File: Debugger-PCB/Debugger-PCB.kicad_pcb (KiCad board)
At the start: 2 copper layers, 64.8 x 48.1 mm, 56 parts, among them J1 Conn_01x04, J2 Conn_01x04, J3 Conn_01x02, J4 USB_C_Receptacle_USB2.0, SW3 SW_Push, SW4 SW_Push, SW5 SW_Push, U1 HX9193, U2 HX9193, U3 CH340E, U4 TJA1051T-3, U5 STM32F103RCTx, U6 XPT2046TS, U7 W25Q32JVSS, Y1 12M

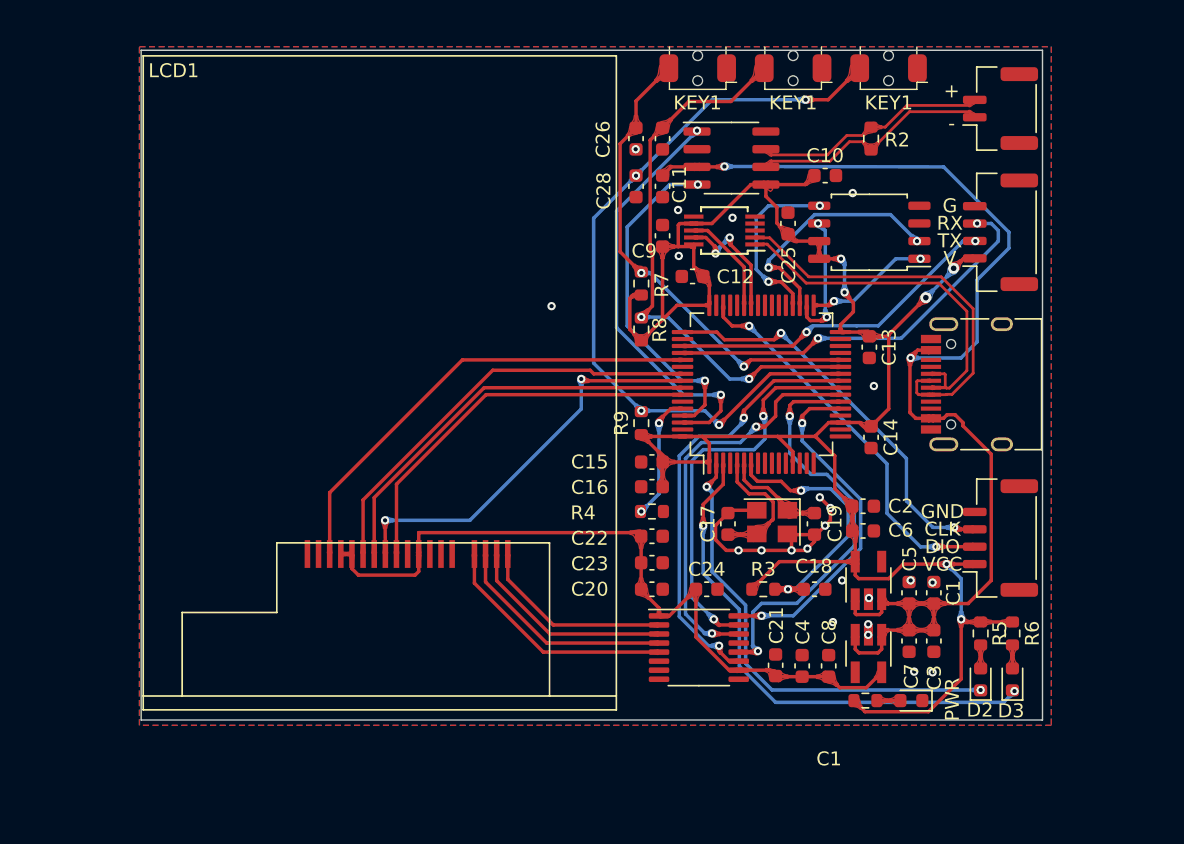
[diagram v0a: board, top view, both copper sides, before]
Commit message: fix some details of PCB
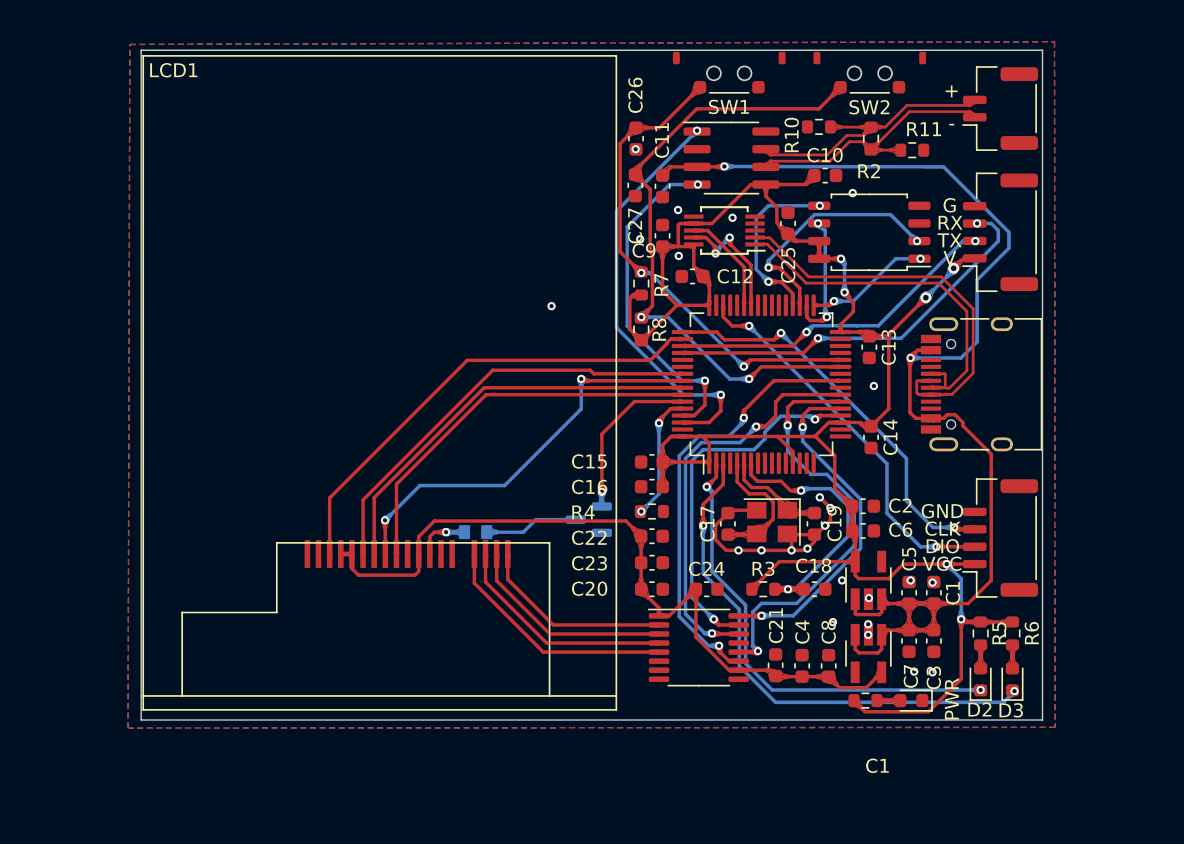
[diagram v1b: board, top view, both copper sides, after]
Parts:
- removed  : 100n, Capacitor_SMD:C_0603_1608Metric
- removed C28: 100n, Capacitor_SMD:C_0603_1608Metric
- removed R9: 1k, Resistor_SMD:R_0603_1608Metric
- removed SW5: SW_Push, MyLib:SW_YD-3410
- added C27: 100n, Capacitor_SMD:C_0603_1608Metric, F.Cu at (152.5, 93.3)
- added Q1: S8050, Package_TO_SOT_SMD:SOT-23, B.Cu at (149.1, 117.3)
- added R10: 10k, Resistor_SMD:R_0603_1608Metric, F.Cu at (165.7, 89.1)
- added R11: 10k, Resistor_SMD:R_0603_1608Metric, F.Cu at (172.4, 90.8)
- added R12: R, GENERAL_RCL_SMD:L0603(1608M), B.Cu at (141.0, 118.2)
- SW1: renamed from SW3; footprint MyLib:SW_YD-3410 -> debugger:button
- SW2: renamed from SW4; footprint MyLib:SW_YD-3410 -> debugger:button
- moved SW2 5.52 mm to (169.3, 85.2)
- moved SW1 2.30 mm to (159.2, 85.2)
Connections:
- LCD1 pad 3: GND -> /TFT/LED-
- U5 pad 20: unconnected-(U5-Pad20) -> /MCU/TOUCH_CS
- U5 pad 24: /MCU/TOUCH_CS -> unconnected-(U5-Pad24)
- U5 pad 26: /Key&LED/KEY3 -> /MCU/KEY3
- U5 pad 50: unconnected-(U5-Pad50) -> /MCU/LCD_CS
- U5 pad 53: /MCU/LCD_CS -> unconnected-(U5-Pad53)
- U5 pad 59: unconnected-(U5-Pad59) -> /MCU/LCD_LED
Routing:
- net /Key&LED/KEY3: track 55.1 -> 0.00 mm, vias 4 -> 0
- net /MCU/LCD_LED: track 0.00 -> 12.0 mm, vias 0 -> 1
- net Net-(Q1-Pad3): track 0.00 -> 6.76 mm
- net /Key&LED/KEY2: track 40.0 -> 45.1 mm
- net /TFT/LED-: track 0.00 -> 3.87 mm, vias 0 -> 1
- net VCC: track 150.1 -> 146.8 mm
- net /Power&Port/CAN+: track 16.8 -> 19.7 mm
- net /MCU/TOUCH_CS: track 28.6 -> 26.5 mm
- net /Power&Port/CAN-: track 17.3 -> 19.5 mm
- net LCD_3V3: track 54.3 -> 55.2 mm
- net /Key&LED/KEY1: track 34.2 -> 34.8 mm
- net GND: vias 23 -> 24
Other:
- board text removed: "KEY1"

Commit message: Finish the GUI
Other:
- board text added: "V2.0"
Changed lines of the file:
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@@
     )
     (fp_line (start -1.4 -1.4) (end 1.4 -1.4) (layer "F.SilkS") (width 0.12))
-    (fp_circle (center -1.1 0) (end -0.6 0) (layer "Edge.Cuts") (width 0.12) (fill none))
-    (fp_circle (center 1.1 0) (end 1.6 0) (layer "Edge.Cuts") (width 0.12) (fill none))
-    (fp_line (start 4.1 -1.7) (end 4.1 2.1) (layer "F.CrtYd") (width 0.05))
-    (fp_line (start -4.1 2.1) (end 4.1 2.1) (layer "F.CrtYd") (width 0.05))
+    (fp_circle (center 1.1 0.1) (end 1.6 0.1) (layer "Edge.Cuts") (width 0.12) (fill none))
+    (fp_circle (center -1.1 0.1) (end -0.6 0.1) (layer "Edge.Cuts") (width 0.12) (fill none))
     (fp_line (start -4.1 -1.7) (end -4.1 2.1) (layer "F.CrtYd") (width 0.05))
     (fp_line (start -4.1 -1.7) (end 4.1 -1.7) (layer "F.CrtYd") (width 0.05))
+    (fp_line (start -4.1 2.1) (end 4.1 2.1) (layer "F.CrtYd") (width 0.05))
+    (fp_line (start 4.1 -1.7) (end 4.1 2.1) (layer "F.CrtYd") (width 0.05))
     (fp_line (start -1.5 2.032) (end -1.5 1.3) (layer "User.1") (width 0.12))
     (fp_line (start -1.5 2.032) (end 1.5 2.032) (layer "User.1") (width 0.12))
+    (fp_line (start -3.5 1.1) (end 3.5 1.1) (layer "User.1") (width 0.12))
     (fp_line (start 1.5 2.032) (end 1.5 1.3) (layer "User.1") (width 0.12))
-    (fp_line (start -3.5 1.1) (end 3.5 1.1) (layer "User.1") (width 0.12))
     (pad "1" smd roundrect (at -2.1 -1 180) (size 0.9 0.9) (layers "F.Cu" "F.Paste" "F.Mask") (roundrect_rratio 0.25)
       (net 2 "GND") (pinfunction "1") (pintype "passive"))
@@
     )
     (fp_line (start -1.4 -1.4) (end 1.4 -1.4) (layer "F.SilkS") (width 0.12))
-    (fp_circle (center -1.1 0) (end -0.6 0) (layer "Edge.Cuts") (width 0.12) (fill none))
-    (fp_circle (center 1.1 0) (end 1.6 0) (layer "Edge.Cuts") (width 0.12) (fill none))
+    (fp_circle (center -1.1 0.1) (end -0.6 0.1) (layer "Edge.Cuts") (width 0.12) (fill none))
+    (fp_circle (center 1.1 0.1) (end 1.6 0.1) (layer "Edge.Cuts") (width 0.12) (fill none))
+    (fp_line (start -4.1 -1.7) (end -4.1 2.1) (layer "F.CrtYd") (width 0.05))
+    (fp_line (start 4.1 -1.7) (end 4.1 2.1) (layer "F.CrtYd") (width 0.05))
+    (fp_line (start -4.1 -1.7) (end 4.1 -1.7) (layer "F.CrtYd") (width 0.05))
     (fp_line (start -4.1 2.1) (end 4.1 2.1) (layer "F.CrtYd") (width 0.05))
-    (fp_line (start -4.1 -1.7) (end -4.1 2.1) (layer "F.CrtYd") (width 0.05))
-    (fp_line (start -4.1 -1.7) (end 4.1 -1.7) (layer "F.CrtYd") (width 0.05))
-    (fp_line (start 4.1 -1.7) (end 4.1 2.1) (layer "F.CrtYd") (width 0.05))
+    (fp_line (start -1.5 2.032) (end -1.5 1.3) (layer "User.1") (width 0.12))
+    (fp_line (start -1.5 2.032) (end 1.5 2.032) (layer "User.1") (width 0.12))
     (fp_line (start 1.5 2.032) (end 1.5 1.3) (layer "User.1") (width 0.12))
-    (fp_line (start -1.5 2.032) (end 1.5 2.032) (layer "User.1") (width 0.12))
     (fp_line (start -3.5 1.1) (end 3.5 1.1) (layer "User.1") (width 0.12))
-    (fp_line (start -1.5 2.032) (end -1.5 1.3) (layer "User.1") (width 0.12))
     (pad "1" smd roundrect (at -2.1 -1 180) (size 0.9 0.9) (layers "F.Cu" "F.Paste" "F.Mask") (roundrect_rratio 0.25)
       (net 2 "GND") (pinfunction "1") (pintype "passive"))
@@
     (effects (font (size 1 1) (thickness 0.15)))
   )
+  (gr_text "V2.0" (at 154.025 130.8) (layer "F.SilkS")
+    (effects (font (size 1 1) (thickness 0.15)))
+  )

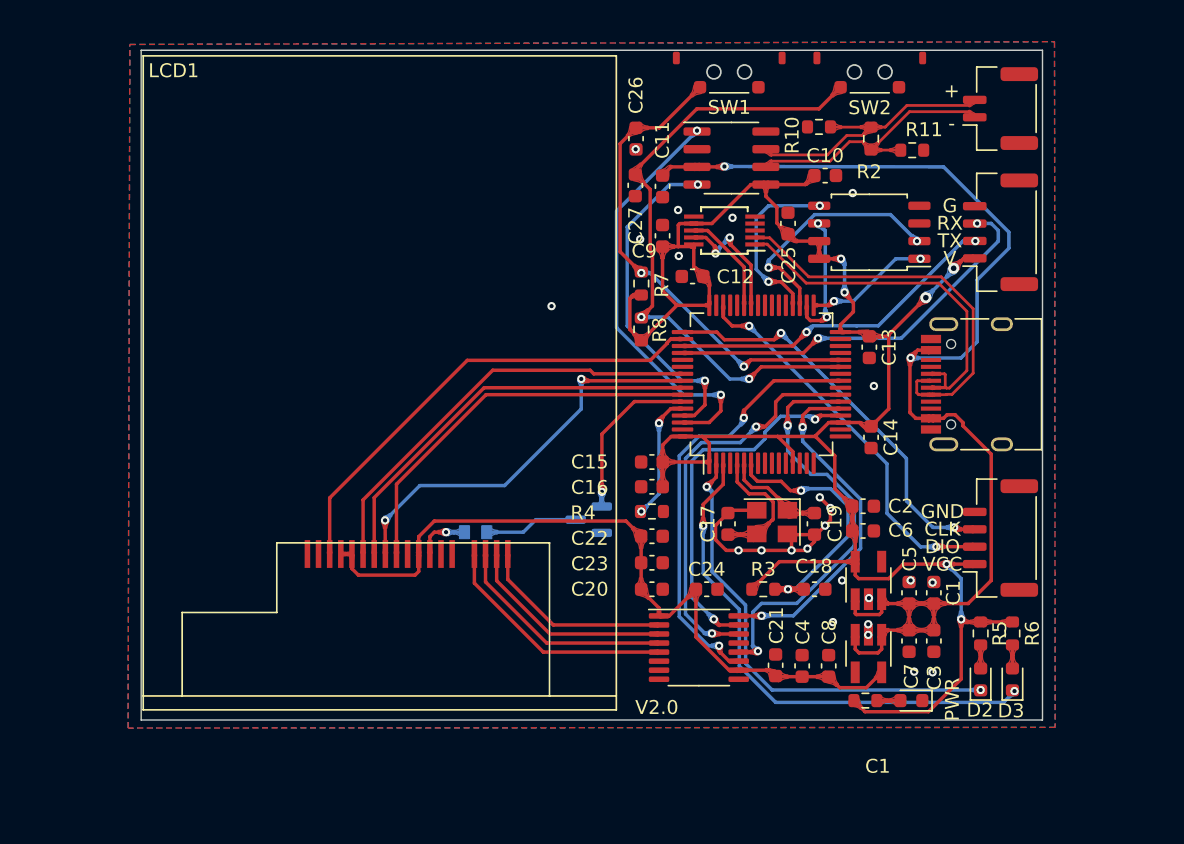
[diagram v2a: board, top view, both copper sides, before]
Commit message: change the file name debugger-code into debugger_code_f103. Change the stm32f103rct6 into stm32f407vet6. Add file debugger_code_f407
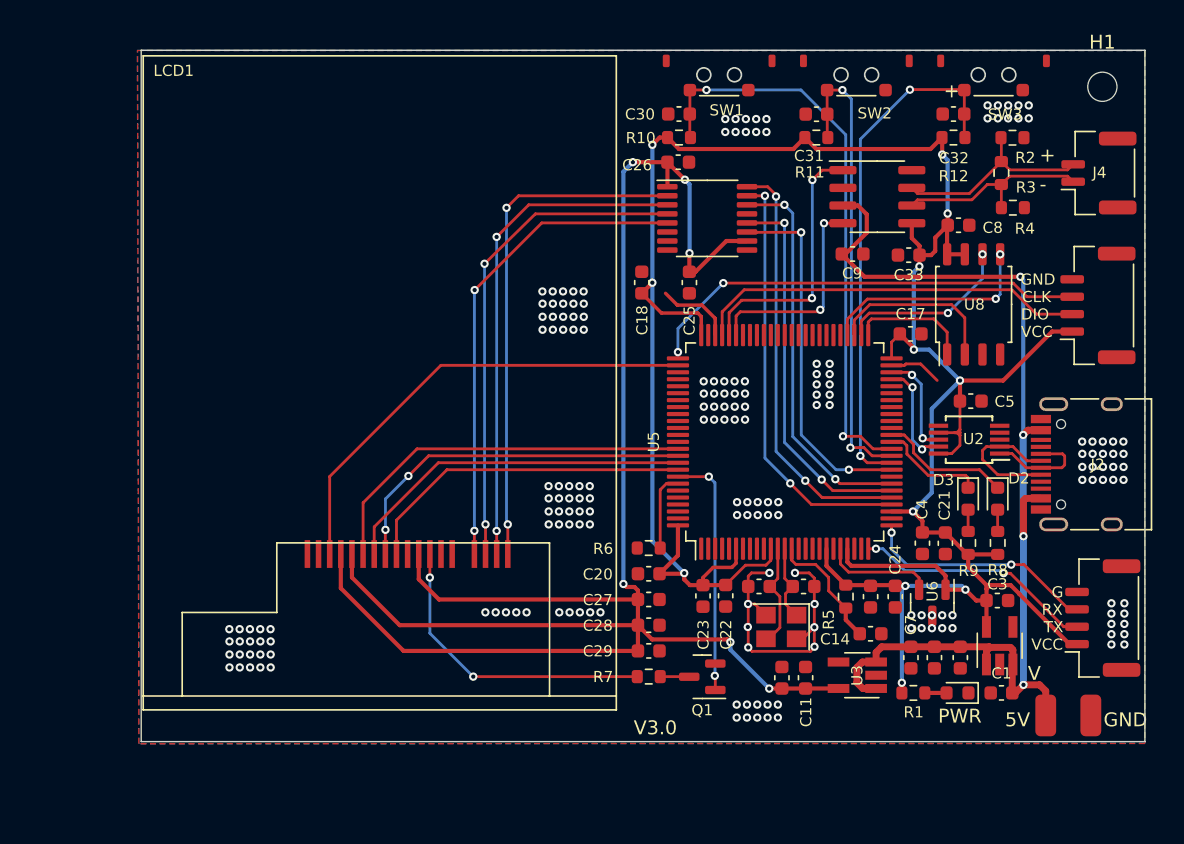
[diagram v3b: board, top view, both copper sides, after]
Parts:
- removed C15, C16: 100n, Capacitor_SMD:C_0603_1608Metric
- added ?: , , F.Cu at (182.0, 131.4)
- added ?: , , F.Cu at (185.2, 131.4)
- added C28: 100n, Capacitor_SMD:C_0603_1608Metric, F.Cu at (153.4, 124.9)
- added C29: 100n, Capacitor_SMD:C_0603_1608Metric, F.Cu at (153.4, 126.7)
- added C30: 100n, Capacitor_SMD:C_0603_1608Metric, F.Cu at (155.6, 88.2)
- added C31: 100n, Capacitor_SMD:C_0603_1608Metric, F.Cu at (165.5, 88.2)
- added C32: 100n, Capacitor_SMD:C_0603_1608Metric, F.Cu at (175.3, 88.2)
- added C33: 100n, Capacitor_SMD:C_0603_1608Metric, F.Cu at (172.1, 98.3)
- added H1: mountinghole, MountingHole:MountingHole_2.1mm, F.Cu at (186.0, 86.2)
- added R9: 1k, Resistor_SMD:R_0603_1608Metric, F.Cu at (176.4, 119.0)
- added SW3: SW_Push, debugger:button, F.Cu at (178.2, 85.4)
- added U8: W25Q32JVSS, Package_SO:SOIC-8_5.23x5.23mm_P1.27mm, F.Cu at (176.8, 101.8)
- C11, C6: value 100n -> 10u
- C12, C13: value 100n -> 12p
- C17, C19: value 12p -> 100n
- C2, C3: value 10u -> 100n
- J2: value Conn_01x04 -> USB_C_Receptacle_USB2.0; footprint Connector_JST:JST_GH_SM04B-GHS-TB_1x04-1MP_P1.25mm_Horizontal -> Connector_USB:USB_C_Receptacle_HRO_TYPE-C-31-M-12
- J3: value Conn_01x02 -> Conn_01x04; footprint Connector_JST:JST_GH_SM02B-GHS-TB_1x02-1MP_P1.25mm_Horizontal -> Connector_JST:JST_GH_SM04B-GHS-TB_1x04-1MP_P1.25mm_Horizontal
- J4: value USB_C_Receptacle_USB2.0 -> Conn_01x02; footprint Connector_USB:USB_C_Receptacle_HRO_TYPE-C-31-M-12 -> Connector_JST:JST_GH_SM02B-GHS-TB_1x02-1MP_P1.25mm_Horizontal
- Q1: moved to F.Cu
- R10, R11: value 10k -> 1k
- R12: value R -> 1k; footprint GENERAL_RCL_SMD:L0603(1608M) -> Resistor_SMD:R_0603_1608Metric; moved to F.Cu
- R2: value 120 -> 10k
- R3: value 10k -> 120
- R5: value 1k -> 10k
- R6: value 1k -> 10K
- R7: value 1k -> R
- U2: value HX9193 -> CH340E; footprint Package_TO_SOT_SMD:SOT-23-5_HandSoldering -> Package_SO:MSOP-10_3x3mm_P0.5mm
- U3: value CH340E -> HX9193; footprint Package_SO:MSOP-10_3x3mm_P0.5mm -> Package_TO_SOT_SMD:SOT-23-5_HandSoldering
- U5: value STM32F103RCTx -> STM32F407VETx; footprint Package_QFP:LQFP-64_10x10mm_P0.5mm -> Package_QFP:LQFP-100_14x14mm_P0.5mm
- U6: value XPT2046TS -> REF3030; footprint debugger:TSSOP-16_4.4x5mm_P0.65mm -> Package_TO_SOT_SMD:SOT-23
- U7: value W25Q32JVSS -> XPT2046TS; footprint Package_SO:SOIC-8_5.23x5.23mm_P1.27mm -> debugger:TSSOP-16_4.4x5mm_P0.65mm
- moved R12 44.5 mm to (175.3, 89.8)
- moved C11 36.8 mm to (164.7, 128.7), turned to 90 degrees
- moved C10 36.2 mm to (163.0, 128.7), turned to 90 degrees
- moved R3 34.5 mm to (178.8, 92.4), turned to -90 degrees
- moved R4 33.9 mm to (179.6, 94.9)
- moved U3 33.4 mm to (168.4, 128.5)
- moved C8 33.0 mm to (175.7, 96.1), turned to 0 degrees
- moved R8 29.9 mm to (178.5, 119.0)
- moved C27 29.8 mm to (153.4, 123.0), turned to 0 degrees
- moved J1 28.7 mm to (186.1, 124.4)
- moved R7 28.3 mm to (153.4, 128.6), turned to 0 degrees
- moved R6 26.8 mm to (153.4, 119.3), turned to 0 degrees
- moved C18 25.3 mm to (152.9, 100.3), turned to 90 degrees
- moved C12 23.7 mm to (164.6, 122.1), turned to 0 degrees
- moved C17 18.9 mm to (172.3, 104.0), turned to 0 degrees
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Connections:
- C10 pad 1: VCC -> LCD_3V3
- C11 pad 1: +5V -> LCD_3V3
- C12 pad 1: VCC -> /MCU/OSC_OUT
- C13 pad 1: VCC -> /MCU/OSC_IN
- C14 pad 1: VCC -> GND
- C14 pad 2: GND -> Net-(U5-NRST)
- C17 pad 1: /MCU/OSC_IN -> VCC
- C18 pad 1: GND -> VCC
- C18 pad 2: Net-(C18-Pad2) -> GND
- C19 pad 1: /MCU/OSC_OUT -> VCC
- C2 pad 1: VCC -> +5V
- C20 pad 1: LCD_3V3 -> VCC
- C21 pad 1: LCD_3V3 -> VCC
- C22 pad 1: LCD_3V3 -> VCC
- C23 pad 1: LCD_3V3 -> VCC
- C24 pad 1: LCD_3V3 -> VCC
- C25 pad 1: VCC -> LCD_3V3
- C26 pad 1: /Key&LED/KEY1 -> LCD_3V3
- C27 pad 1: /Key&LED/KEY2 -> LCD_3V3
- C3 pad 1: +5V -> VCC
- C4 pad 1: LCD_3V3 -> VCC
- C5 pad 1: +5V -> VCC
- C6 pad 1: VCC -> +5V
- C8 pad 1: LCD_3V3 -> VCC
- C9 pad 1: VCC -> +5V
- D2 pad 2: Net-(D2-Pad2) -> Net-(D2-A)
- D3 pad 2: Net-(D3-Pad2) -> Net-(D3-A)
- J3 pad 1: /Power&Port/CAN- -> VCC
- J3 pad 2: /Power&Port/CAN+ -> /MCU/SWDIO
- Q1 pad 3: Net-(Q1-Pad3) -> Net-(Q1-C)
- R10 pad 1: GND -> VCC
- R10 pad 2: /Power&Port/CAN+ -> /Key&LED/KEY1
- R11 pad 1: /Power&Port/CAN- -> VCC
- R11 pad 2: GND -> /Key&LED/KEY2
- R12 pad 1: /TFT/LED- -> VCC
- R12 pad 2: Net-(Q1-Pad3) -> /Key&LED/KEY3
- R2 pad 1: /Power&Port/CAN+ -> GND
- R2 pad 2: /Power&Port/CAN- -> /Power&Port/CAN+
- R3 pad 1: VCC -> /Power&Port/CAN+
- R3 pad 2: Net-(C18-Pad2) -> /Power&Port/CAN-
- R4 pad 1: Net-(R4-Pad1) -> /Power&Port/CAN-
- R5 pad 2: Net-(D2-Pad2) -> Net-(U5-NRST)
- R6 pad 1: VCC -> GND
- R6 pad 2: Net-(D3-Pad2) -> Net-(U5-BOOT0)
- R7 pad 1: VCC -> /TFT/LED-
- R7 pad 2: /Key&LED/KEY1 -> Net-(Q1-C)
- R8 pad 2: /Key&LED/KEY2 -> Net-(D2-A)
- U2 pad 1: +5V -> /Power&Port/DP
- U2 pad 2: GND -> /Power&Port/DN
- U2 pad 3: +5V -> GND
- U2 pad 5: LCD_3V3 -> unconnected-(U2-~{CTS}-Pad5)
- U3 pad 1: /Power&Port/DP -> +5V
- U3 pad 2: /Power&Port/DN -> GND
- U3 pad 3: GND -> +5V
- U3 pad 5: unconnected-(U3-Pad5) -> LCD_3V3
- U5 pad 1: VCC -> unconnected-(U5-PE2-Pad1)
- U5 pad 10: unconnected-(U5-Pad10) -> GND
- U5 pad 11: unconnected-(U5-Pad11) -> VCC
- U5 pad 12: GND -> /MCU/OSC_IN
- U5 pad 13: VCC -> /MCU/OSC_OUT
- U5 pad 14: unconnected-(U5-Pad14) -> Net-(U5-NRST)
- U5 pad 18: GND -> unconnected-(U5-PC3-Pad18)
- U5 pad 2: /Key&LED/LED1 -> unconnected-(U5-PE3-Pad2)
- U5 pad 20: /MCU/TOUCH_CS -> GND
- U5 pad 21: /MCU/TOUCH_CLK -> /MCU/VREF
- U5 pad 22: /MCU/TOUCH_MISO -> VCC
- U5 pad 23: /MCU/TOUCH_MOSI -> unconnected-(U5-PA0-Pad23)
- U5 pad 25: /MCU/TOUCH_INT -> /MCU/TXD
- U5 pad 26: /MCU/KEY3 -> /MCU/RXD
- U5 pad 27: /Key&LED/KEY2 -> GND
- U5 pad 28: /Key&LED/KEY1 -> VCC
- U5 pad 29: unconnected-(U5-Pad29) -> /MCU/TOUCH_CS
- U5 pad 3: /Key&LED/LED2 -> unconnected-(U5-PE4-Pad3)
- U5 pad 30: unconnected-(U5-Pad30) -> /MCU/TOUCH_CLK
- U5 pad 31: GND -> /MCU/TOUCH_MISO
- U5 pad 32: VCC -> /MCU/TOUCH_MOSI
- U5 pad 33: /Flash/SPI2_CS -> unconnected-(U5-PC4-Pad33)
- U5 pad 34: /Flash/SPI2_SCK -> /MCU/TOUCH_INT
- U5 pad 35: /Flash/SPI2_MISO -> /Key&LED/KEY3
- U5 pad 36: /Flash/SPI2_MOSI -> /Key&LED/KEY2
- U5 pad 37: unconnected-(U5-Pad37) -> /Key&LED/KEY1
- U5 pad 38: unconnected-(U5-Pad38) -> /Key&LED/LED2
- U5 pad 39: unconnected-(U5-Pad39) -> /Key&LED/LED1
- U5 pad 42: /MCU/MCU_TXD -> unconnected-(U5-PE11-Pad42)
- U5 pad 43: /MCU/MCU_RXD -> unconnected-(U5-PE12-Pad43)
- U5 pad 46: /MCU/SWDIO -> unconnected-(U5-PE15-Pad46)
- U5 pad 47: GND -> /MCU/MCU_TXD
- U5 pad 48: VCC -> /MCU/MCU_RXD
- U5 pad 49: /MCU/SWCLK -> Net-(U5-VCAP_1)
- U5 pad 5: /MCU/OSC_IN -> unconnected-(U5-PE6-Pad5)
- U5 pad 50: /MCU/LCD_CS -> VCC
- U5 pad 51: /MCU/TXD -> /Flash/SPI2_CS
- U5 pad 52: /MCU/RXD -> /Flash/SPI2_SCK
- U5 pad 53: unconnected-(U5-Pad53) -> /Flash/SPI2_MISO
- U5 pad 54: unconnected-(U5-Pad54) -> /Flash/SPI2_MOSI
- U5 pad 55: /MCU/LCD_CLK -> unconnected-(U5-PD8-Pad55)
- U5 pad 56: /MCU/LCD_A0 -> unconnected-(U5-PD9-Pad56)
- U5 pad 57: /MCU/LCD_MOSI -> unconnected-(U5-PD10-Pad57)
- U5 pad 58: /MCU/LCD_RST -> unconnected-(U5-PD11-Pad58)
- U5 pad 59: /MCU/LCD_LED -> unconnected-(U5-PD12-Pad59)
- U5 pad 6: /MCU/OSC_OUT -> VCC
- U5 pad 60: Net-(R4-Pad1) -> unconnected-(U5-PD13-Pad60)
- U5 pad 61: /MCU/CAN_RX -> unconnected-(U5-PD14-Pad61)
- U5 pad 62: /MCU/CAN_TX -> unconnected-(U5-PD15-Pad62)
- U5 pad 63: GND -> unconnected-(U5-PC6-Pad63)
- U5 pad 64: VCC -> unconnected-(U5-PC7-Pad64)
- U5 pad 7: Net-(C18-Pad2) -> unconnected-(U5-PC13-Pad7)
- U6 pad 1: LCD_3V3 -> VCC
- U6 pad 2: /TFT/T_XP -> /MCU/VREF
- U6 pad 3: /TFT/T_YP -> GND
- U7 pad 1: /Flash/SPI2_CS -> LCD_3V3
- U7 pad 2: /Flash/SPI2_MISO -> /TFT/T_XP
- U7 pad 3: GND -> /TFT/T_YP
- U7 pad 4: GND -> /TFT/T_XM
- U7 pad 5: /Flash/SPI2_MOSI -> /TFT/T_YM
- U7 pad 6: /Flash/SPI2_SCK -> GND
- U7 pad 7: VCC -> unconnected-(U7-VBAT-Pad7)
- U7 pad 8: VCC -> unconnected-(U7-IN-Pad8)
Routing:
- net LCD_3V3: track 55.2 -> 138.2 mm, vias 0 -> 6
- net VCC: track 146.8 -> 196.2 mm, vias 6 -> 12
- net /Key&LED/KEY3: track 0.00 -> 37.6 mm, vias 0 -> 2
- net /Key&LED/LED2: track 37.5 -> 7.64 mm, vias 2 -> 0
- net /Key&LED/LED1: track 33.5 -> 9.55 mm, vias 2 -> 0
- net /TFT/T_XP: track 14.0 -> 36.8 mm, vias 0 -> 2
- net /TFT/T_YP: track 15.2 -> 36.0 mm, vias 0 -> 2
- net /Power&Port/DP: track 27.6 -> 7.59 mm
- net /TFT/T_XM: track 16.3 -> 35.5 mm, vias 0 -> 2
- net /Power&Port/DN: track 29.0 -> 10.0 mm
- net Net-(C18-Pad2): track 19.0 -> 0.00 mm, vias 2 -> 0
- net /TFT/LED-: track 3.87 -> 21.9 mm, vias 1 -> 2
- net /TFT/T_YM: track 17.4 -> 34.8 mm, vias 0 -> 2
- net /MCU/RXD: track 28.5 -> 16.9 mm
- net /Key&LED/KEY2: track 45.1 -> 33.7 mm
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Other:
- board size 64.8 x 48.1 mm -> 72.1 x 49.7 mm
- board text added: "5V"
- board text added: "V3.0"
- board text removed: "C1"
- board text removed: "V2.0"
